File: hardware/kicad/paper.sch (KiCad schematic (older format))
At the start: 30 parts

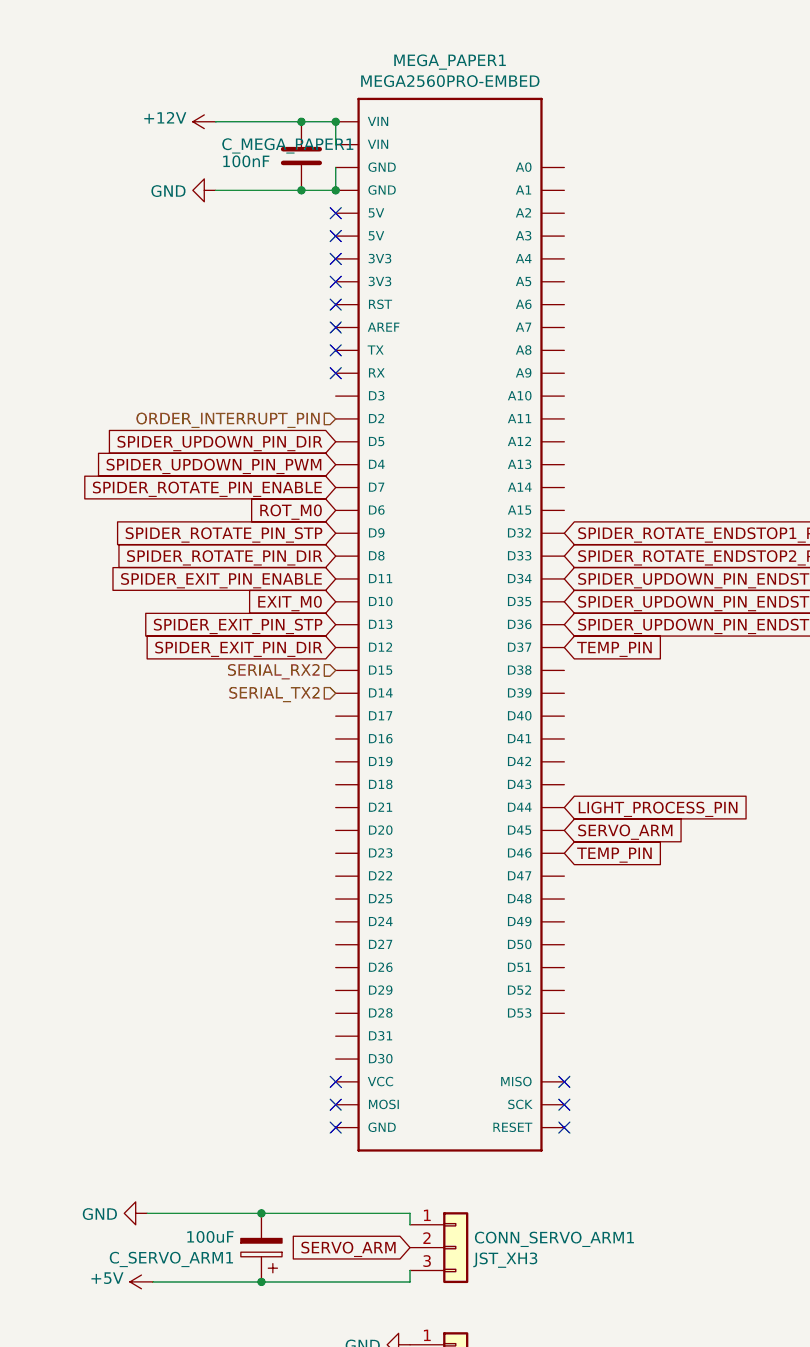
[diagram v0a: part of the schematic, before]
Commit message: correction schematic gilou
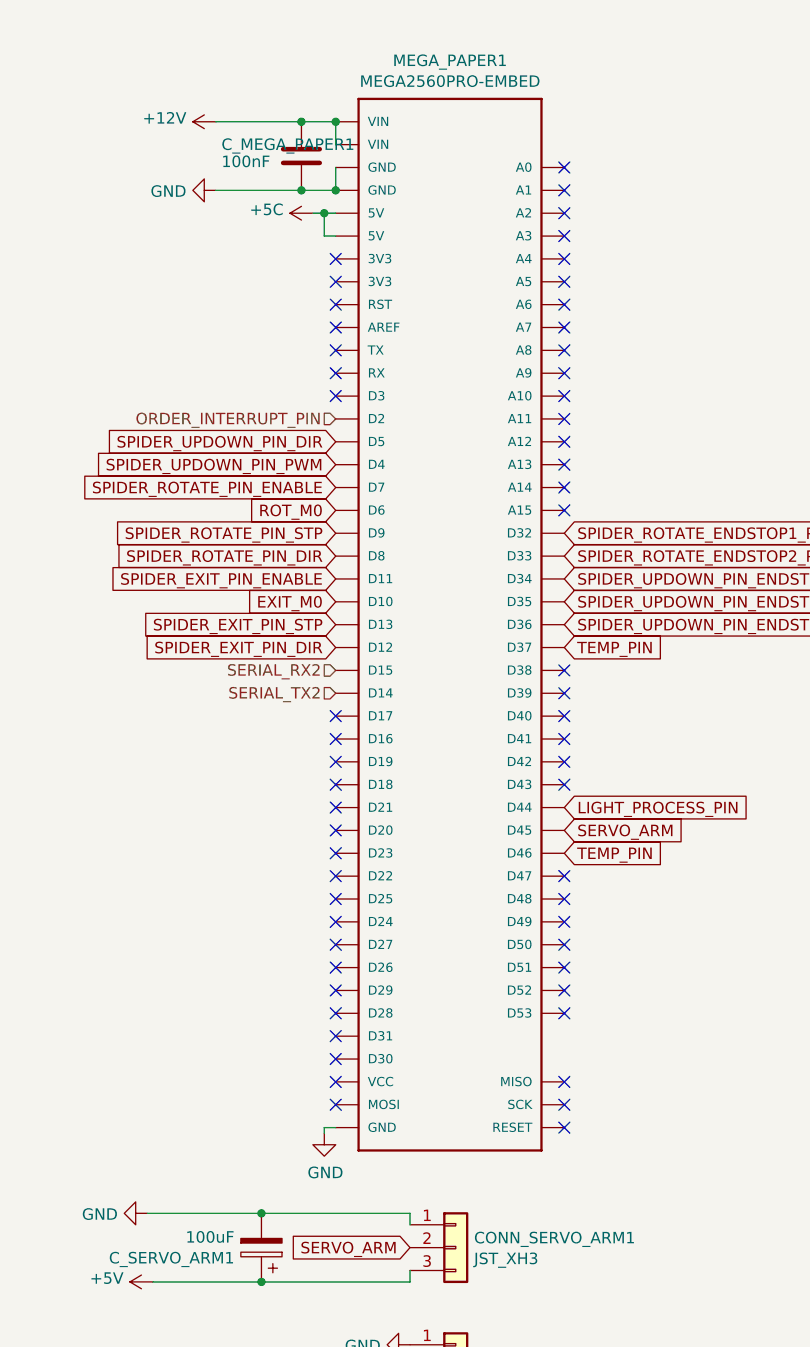
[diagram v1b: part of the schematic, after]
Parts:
- C_MEGA_PAPER1: footprint Capacitor_THT:C_Disc_D3.0mm_W1.6mm_P2.50mm -> Capacitor_THT:C_Rect_L7.2mm_W2.5mm_P5.00mm_FKS2_FKP2_MKS2_MKP2
- R_SW_BOTTOM1, R_SW_MIDDLE1, R_SW_ROT1, R_SW_ROT2, R_SW_UP1: footprint Resistor_THT:R_Axial_DIN0309_L9.0mm_D3.2mm_P12.70mm_Horizontal -> Resistor_THT:R_Axial_DIN0207_L6.3mm_D2.5mm_P10.16mm_Horizontal
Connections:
- net +5C: now reaches MEGA_PAPER1.5V
- no-connect marks 16 -> 59
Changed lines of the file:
@@
 F 0 "R_SW_ROT1" V 9379 925 50  0000 C CNN
 F 1 "560ohm 1/2W" V 9470 925 50  0000 C CNN
-F 2 "Resistor_THT:R_Axial_DIN0309_L9.0mm_D3.2mm_P12.70mm_Horizontal" H 9575 925 50  0001 C CNN
+F 2 "Resistor_THT:R_Axial_DIN0207_L6.3mm_D2.5mm_P10.16mm_Horizontal" H 9575 925 50  0001 C CNN
 F 3 "~" H 9575 925 50  0001 C CNN
 	1    9575 925
@@
 F 0 "R_SW_ROT2" V 9329 1775 50  0000 C CNN
 F 1 "560ohm 1/2W" V 9420 1775 50  0000 C CNN
-F 2 "Resistor_THT:R_Axial_DIN0309_L9.0mm_D3.2mm_P12.70mm_Horizontal" H 9525 1775 50  0001 C CNN
+F 2 "Resistor_THT:R_Axial_DIN0207_L6.3mm_D2.5mm_P10.16mm_Horizontal" H 9525 1775 50  0001 C CNN
 F 3 "~" H 9525 1775 50  0001 C CNN
 	1    9525 1775
@@
 F 0 "R_SW_UP1" V 9504 2725 50  0000 C CNN
 F 1 "560ohm 1/2W" V 9595 2725 50  0000 C CNN
-F 2 "Resistor_THT:R_Axial_DIN0309_L9.0mm_D3.2mm_P12.70mm_Horizontal" H 9700 2725 50  0001 C CNN
+F 2 "Resistor_THT:R_Axial_DIN0207_L6.3mm_D2.5mm_P10.16mm_Horizontal" H 9700 2725 50  0001 C CNN
 F 3 "~" H 9700 2725 50  0001 C CNN
 	1    9700 2725
@@
 F 0 "R_SW_MIDDLE1" V 9579 3750 50  0000 C CNN
 F 1 "560ohm 1/2W" V 9670 3750 50  0000 C CNN
-F 2 "Resistor_THT:R_Axial_DIN0309_L9.0mm_D3.2mm_P12.70mm_Horizontal" H 9775 3750 50  0001 C CNN
+F 2 "Resistor_THT:R_Axial_DIN0207_L6.3mm_D2.5mm_P10.16mm_Horizontal" H 9775 3750 50  0001 C CNN
 F 3 "~" H 9775 3750 50  0001 C CNN
 	1    9775 3750
@@
 F 0 "R_SW_BOTTOM1" V 9579 4550 50  0000 C CNN
 F 1 "560ohm 1/2W" V 9670 4550 50  0000 C CNN
-F 2 "Resistor_THT:R_Axial_DIN0309_L9.0mm_D3.2mm_P12.70mm_Horizontal" H 9775 4550 50  0001 C CNN
+F 2 "Resistor_THT:R_Axial_DIN0207_L6.3mm_D2.5mm_P10.16mm_Horizontal" H 9775 4550 50  0001 C CNN
 F 3 "~" H 9775 4550 50  0001 C CNN
 	1    9775 4550
@@
 Wire Wire Line
 	4900 6450 5550 6450
-NoConn ~ 5225 1775
-NoConn ~ 5225 1875
 NoConn ~ 5225 1975
 NoConn ~ 5225 2075
@@
 NoConn ~ 5225 5575
 NoConn ~ 5225 5675
-NoConn ~ 5225 5775
 NoConn ~ 6225 5575
 NoConn ~ 6225 5675
@@
 F 0 "C_MEGA_PAPER1" H 4725 1575 50  0000 L CNN
 F 1 "100nF" H 4725 1500 50  0000 L CNN
-F 2 "Capacitor_THT:C_Disc_D3.0mm_W1.6mm_P2.50mm" H 5113 1375 50  0001 C CNN
+F 2 "Capacitor_THT:C_Rect_L7.2mm_W2.5mm_P5.00mm_FKS2_FKP2_MKS2_MKP2" H 5113 1375 50  0001 C CNN
 F 3 "~" H 5075 1525 50  0001 C CNN
 	1    5075 1525
@@
 Wire Wire Line
 	1500 6200 1825 6200
+NoConn ~ 6225 1575
+NoConn ~ 6225 1675
+NoConn ~ 6225 1775
+NoConn ~ 6225 1875
+NoConn ~ 6225 1975
+NoConn ~ 6225 2075
+NoConn ~ 6225 2175
+NoConn ~ 6225 2275
+NoConn ~ 6225 2375
+NoConn ~ 6225 2475
+NoConn ~ 6225 2575
+NoConn ~ 6225 2675
+NoConn ~ 6225 2775
+NoConn ~ 6225 2875
+NoConn ~ 6225 2975
+NoConn ~ 6225 3075
+NoConn ~ 6225 3775
+NoConn ~ 6225 3875
+NoConn ~ 6225 3975
+NoConn ~ 6225 4075
+NoConn ~ 6225 4175
+NoConn ~ 6225 4275
+NoConn ~ 6225 4675
+NoConn ~ 6225 4775
+NoConn ~ 6225 4875
+NoConn ~ 6225 4975
+NoConn ~ 6225 5075
+NoConn ~ 6225 5175
+NoConn ~ 6225 5275
+NoConn ~ 5225 5475
+NoConn ~ 5225 5375
+NoConn ~ 5225 5275
+NoConn ~ 5225 5175
+NoConn ~ 5225 5075
+NoConn ~ 5225 4975
+NoConn ~ 5225 4875
+NoConn ~ 5225 4775
+NoConn ~ 5225 4675
+NoConn ~ 5225 4575
+NoConn ~ 5225 4475
+NoConn ~ 5225 4375
+NoConn ~ 5225 4275
+NoConn ~ 5225 4075
+NoConn ~ 5225 3975
+NoConn ~ 5225 4175
+NoConn ~ 5225 2575
+$Comp
+L power:GND #PWR0209
+U 1 1 5E497F5C
+P 5175 5800
+F 0 "#PWR0209" H 5175 5550 50  0001 C CNN
+F 1 "GND" H 5180 5627 50  0000 C CNN
+F 2 "" H 5175 5800 50  0001 C CNN
+F 3 "" H 5175 5800 50  0001 C CNN
+	1    5175 5800
+	1    0    0    -1
+$EndComp
+Wire Wire Line
+	5175 5800 5175 5775
+Wire Wire Line
+	5175 5775 5225 5775
+$Comp
+L power:+5C #PWR?
+U 1 1 5E4E76A1
+P 5125 1775
+AR Path="/5E3BF423/5E4E76A1" Ref="#PWR?"  Part="1"
+AR Path="/5E432787/5E4E76A1" Ref="#PWR0212"  Part="1"
+F 0 "#PWR0212" H 5125 1625 50  0001 C CNN
+F 1 "+5C" V 5140 1903 50  0000 L CNN
+F 2 "" H 5125 1775 50  0001 C CNN
+F 3 "" H 5125 1775 50  0001 C CNN
+	1    5125 1775
+	0    -1   -1   0
+$EndComp
+Wire Wire Line
+	5125 1775 5175 1775
+Wire Wire Line
+	5225 1875 5175 1875
+Wire Wire Line
+	5175 1875 5175 1775
+Connection ~ 5175 1775
+Wire Wire Line
+	5175 1775 5225 1775
 $EndSCHEMATC

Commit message: update, gilou dans la place
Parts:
- added CONN_FAN1: JST_XH2, Connector_JST:JST_XH_S2B-XH-A-1_1x02_P2.50mm_Horizontal, symbol 1nofilterbooth:Conn_01x02-Connector_Generic
- added C_AUX3: 680uF, Capacitor_THT:CP_Radial_D8.0mm_P3.50mm, symbol 1nofilterbooth:CP-Device
- added Q_AUX2: TIP120, Package_TO_SOT_THT:TO-220-3_Vertical, symbol 1nofilterbooth:TIP120-Transistor_BJT
- added R_FLASH4: 2.2k 1/2W, Resistor_THT:R_Axial_DIN0207_L6.3mm_D2.5mm_P10.16mm_Horizontal, symbol 1nofilterbooth:R_Small-Device
- CONN_DC1, CONN_SW_BOTTOM1, CONN_SW_MIDDLE1, CONN_SW_UP1: footprint Connector_JST:JST_XH_S2B-XH-A_1x02_P2.50mm_Horizontal -> Connector_JST:JST_XH_S2B-XH-A-1_1x02_P2.50mm_Horizontal
- CONN_LGHT_PROCESS1, CONN_SERVO_ARM1, CONN_SW_ROT1, CONN_SW_ROT2, CONN_TEMP1: footprint Connector_JST:JST_XH_S3B-XH-A_1x03_P2.50mm_Horizontal -> Connector_JST:JST_XH_S3B-XH-A-1_1x03_P2.50mm_Horizontal
- CONN_STEP_EXIT1, CONN_STEP_ROT1: value Conn_01x04 -> JST_XH4; footprint Connector_JST:JST_XH_S4B-XH-A_1x04_P2.50mm_Horizontal -> Connector_JST:JST_XH_S4B-XH-A-1_1x04_P2.50mm_Horizontal
- C_LIGHT_PROCESS1: value 1000uF -> 100uF; footprint Capacitor_THT:CP_Radial_D10.0mm_P5.00mm -> Capacitor_THT:CP_Radial_D6.3mm_P2.50mm
- C_ROT1, C_SERVO_ARM1, C_STEP1: footprint Capacitor_THT:CP_Radial_D10.0mm_P5.00mm -> Capacitor_THT:CP_Radial_D6.3mm_P2.50mm
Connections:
- net +12V: now also CONN_FAN1.1 (Pin_1), C_AUX3.2
- net GND: now also C_AUX3.1, Q_AUX2.3 (E)
- net FAN_PIN: now reaches MEGA_PAPER1.D39
- net FAN_PIN: now also R_FLASH4.2
- net at DRV_DC1.A: now also CONN_DC1.1 (Pin_1); no longer CONN_DC1.2 (Pin_2)
- net at DRV_DC1.B: now also CONN_DC1.2 (Pin_2); no longer CONN_DC1.1 (Pin_1)
- net +5C: no longer names the net of MEGA_PAPER1.5V
- new net: CONN_FAN1.2 (Pin_2), Q_AUX2.2 (C)
- new net: Q_AUX2.1 (B), R_FLASH4.1
- no-connect marks 59 -> 60
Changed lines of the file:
@@
 AR Path="/5E432787/5E421575" Ref="CONN_STEP_ROT1"  Part="1"
 F 0 "CONN_STEP_ROT1" H 1243 1325 50  0000 C CNN
-F 1 "Conn_01x04" H 1243 1416 50  0000 C CNN
-F 2 "Connector_JST:JST_XH_S4B-XH-A_1x04_P2.50mm_Horizontal" H 1325 1750 50  0001 C CNN
+F 1 "JST_XH4" H 1243 1416 50  0000 C CNN
+F 2 "Connector_JST:JST_XH_S4B-XH-A-1_1x04_P2.50mm_Horizontal" H 1325 1750 50  0001 C CNN
 F 3 "~" H 1325 1750 50  0001 C CNN
 	1    1325 1750
@@
 F 0 "C_ROT1" H 2643 2596 50  0000 L CNN
 F 1 "100uF" H 2643 2505 50  0000 L CNN
-F 2 "Capacitor_THT:CP_Radial_D10.0mm_P5.00mm" H 2563 2400 50  0001 C CNN
+F 2 "Capacitor_THT:CP_Radial_D6.3mm_P2.50mm" H 2563 2400 50  0001 C CNN
 F 3 "~" H 2525 2550 50  0001 C CNN
 	1    2525 2550
@@
 AR Path="/5E432787/5E43ED6E" Ref="CONN_STEP_EXIT1"  Part="1"
 F 0 "CONN_STEP_EXIT1" H 1193 3475 50  0000 C CNN
-F 1 "Conn_01x04" H 1193 3566 50  0000 C CNN
-F 2 "Connector_JST:JST_XH_S4B-XH-A_1x04_P2.50mm_Horizontal" H 1275 3900 50  0001 C CNN
+F 1 "JST_XH4" H 1193 3566 50  0000 C CNN
+F 2 "Connector_JST:JST_XH_S4B-XH-A-1_1x04_P2.50mm_Horizontal" H 1275 3900 50  0001 C CNN
 F 3 "~" H 1275 3900 50  0001 C CNN
 	1    1275 3900
@@
 F 0 "CONN_SW_ROT2" H 10205 2017 50  0000 L CNN
 F 1 "JST_XH3" H 10205 1926 50  0000 L CNN
-F 2 "Connector_JST:JST_XH_S3B-XH-A_1x03_P2.50mm_Horizontal" H 10125 1975 50  0001 C CNN
+F 2 "Connector_JST:JST_XH_S3B-XH-A-1_1x03_P2.50mm_Horizontal" H 10125 1975 50  0001 C CNN
 F 3 "~" H 10125 1975 50  0001 C CNN
 	1    10125 1975
@@
 F 0 "CONN_SW_ROT1" H 10255 1167 50  0000 L CNN
 F 1 "JST_XH3" H 10255 1076 50  0000 L CNN
-F 2 "Connector_JST:JST_XH_S3B-XH-A_1x03_P2.50mm_Horizontal" H 10175 1125 50  0001 C CNN
+F 2 "Connector_JST:JST_XH_S3B-XH-A-1_1x03_P2.50mm_Horizontal" H 10175 1125 50  0001 C CNN
 F 3 "~" H 10175 1125 50  0001 C CNN
 	1    10175 1125
@@
 F 0 "CONN_SW_UP1" H 10180 2917 50  0000 L CNN
 F 1 "JST_XH2" H 10180 2826 50  0000 L CNN
-F 2 "Connector_JST:JST_XH_S2B-XH-A_1x02_P2.50mm_Horizontal" H 10100 2925 50  0001 C CNN
+F 2 "Connector_JST:JST_XH_S2B-XH-A-1_1x02_P2.50mm_Horizontal" H 10100 2925 50  0001 C CNN
 F 3 "~" H 10100 2925 50  0001 C CNN
 	1    10100 2925
@@
 F 0 "CONN_SW_MIDDLE1" H 10255 3942 50  0000 L CNN
 F 1 "JST_XH2" H 10255 3851 50  0000 L CNN
-F 2 "Connector_JST:JST_XH_S2B-XH-A_1x02_P2.50mm_Horizontal" H 10175 3950 50  0001 C CNN
+F 2 "Connector_JST:JST_XH_S2B-XH-A-1_1x02_P2.50mm_Horizontal" H 10175 3950 50  0001 C CNN
 F 3 "~" H 10175 3950 50  0001 C CNN
 	1    10175 3950
@@
 F 0 "CONN_SW_BOTTOM1" H 10255 4742 50  0000 L CNN
 F 1 "JST_XH2" H 10255 4651 50  0000 L CNN
-F 2 "Connector_JST:JST_XH_S2B-XH-A_1x02_P2.50mm_Horizontal" H 10175 4750 50  0001 C CNN
+F 2 "Connector_JST:JST_XH_S2B-XH-A-1_1x02_P2.50mm_Horizontal" H 10175 4750 50  0001 C CNN
 F 3 "~" H 10175 4750 50  0001 C CNN
 	1    10175 4750
@@
 F 0 "CONN_TEMP1" H 5830 6867 50  0000 L CNN
 F 1 "JST_XH3" H 5830 6776 50  0000 L CNN
-F 2 "Connector_JST:JST_XH_S3B-XH-A_1x03_P2.50mm_Horizontal" H 5750 6825 50  0001 C CNN
+F 2 "Connector_JST:JST_XH_S3B-XH-A-1_1x03_P2.50mm_Horizontal" H 5750 6825 50  0001 C CNN
 F 3 "~" H 5750 6825 50  0001 C CNN
 	1    5750 6825
@@
 F 0 "CONN_LGHT_PROCESS1" H 5830 7517 50  0000 L CNN
 F 1 "JST_XH3" H 5830 7426 50  0000 L CNN
-F 2 "Connector_JST:JST_XH_S3B-XH-A_1x03_P2.50mm_Horizontal" H 5750 7475 50  0001 C CNN
+F 2 "Connector_JST:JST_XH_S3B-XH-A-1_1x03_P2.50mm_Horizontal" H 5750 7475 50  0001 C CNN
 F 3 "~" H 5750 7475 50  0001 C CNN
 	1    5750 7475
@@
 F 0 "C_STEP1" H 2593 4746 50  0000 L CNN
 F 1 "100uF" H 2593 4655 50  0000 L CNN
-F 2 "Capacitor_THT:CP_Radial_D10.0mm_P5.00mm" H 2513 4550 50  0001 C CNN
+F 2 "Capacitor_THT:CP_Radial_D6.3mm_P2.50mm" H 2513 4550 50  0001 C CNN
 F 3 "~" H 2475 4700 50  0001 C CNN
 	1    2475 4700
@@
 AR Path="/5E432787/5E480053" Ref="C_LIGHT_PROCESS1"  Part="1"
 F 0 "C_LIGHT_PROCESS1" H 4743 7521 50  0000 L CNN
-F 1 "1000uF" H 4743 7430 50  0000 L CNN
-F 2 "Capacitor_THT:CP_Radial_D10.0mm_P5.00mm" H 4663 7325 50  0001 C CNN
+F 1 "100uF" H 4743 7430 50  0000 L CNN
+F 2 "Capacitor_THT:CP_Radial_D6.3mm_P2.50mm" H 4663 7325 50  0001 C CNN
 F 3 "~" H 4625 7475 50  0001 C CNN
 	1    4625 7475
@@
 F 0 "CONN_SERVO_ARM1" H 5830 6342 50  0000 L CNN
 F 1 "JST_XH3" H 5830 6251 50  0000 L CNN
-F 2 "Connector_JST:JST_XH_S3B-XH-A_1x03_P2.50mm_Horizontal" H 5750 6300 50  0001 C CNN
+F 2 "Connector_JST:JST_XH_S3B-XH-A-1_1x03_P2.50mm_Horizontal" H 5750 6300 50  0001 C CNN
 F 3 "~" H 5750 6300 50  0001 C CNN
 	1    5750 6300
@@
 F 0 "C_SERVO_ARM1" H 5018 6346 50  0000 L CNN
 F 1 "100uF" H 5018 6255 50  0000 L CNN
-F 2 "Capacitor_THT:CP_Radial_D10.0mm_P5.00mm" H 4938 6150 50  0001 C CNN
+F 2 "Capacitor_THT:CP_Radial_D6.3mm_P2.50mm" H 4938 6150 50  0001 C CNN
 F 3 "~" H 4900 6300 50  0001 C CNN
 	1    4900 6300
@@
 Wire Wire Line
 	4900 6450 5550 6450
-NoConn ~ 5225 1975
-NoConn ~ 5225 2075
 NoConn ~ 5225 2175
 NoConn ~ 5225 2275
@@
 L 1nofilterbooth:Conn_01x02-Connector_Generic CONN_SW_MIDDLE?
 U 1 1 5E5BAF8E
-P 1300 6200
+P 1300 6100
 AR Path="/5E5BAF8E" Ref="CONN_SW_MIDDLE?"  Part="1"
 AR Path="/5E3BF423/5E5BAF8E" Ref="CONN_SW_MIDDLE?"  Part="1"
 AR Path="/5E432787/5E5BAF8E" Ref="CONN_DC1"  Part="1"
-F 0 "CONN_DC1" H 1380 6192 50  0000 L CNN
-F 1 "JST_XH2" H 1380 6101 50  0000 L CNN
-F 2 "Connector_JST:JST_XH_S2B-XH-A_1x02_P2.50mm_Horizontal" H 1300 6200 50  0001 C CNN
-F 3 "~" H 1300 6200 50  0001 C CNN
-	1    1300 6200
-	-1   0    0    1
+F 0 "CONN_DC1" H 1380 6092 50  0000 L CNN
+F 1 "JST_XH2" H 1380 6001 50  0000 L CNN
+F 2 "Connector_JST:JST_XH_S2B-XH-A-1_1x02_P2.50mm_Horizontal" H 1300 6100 50  0001 C CNN
+F 3 "~" H 1300 6100 50  0001 C CNN
+	1    1300 6100
+	-1   0    0    -1
 $EndComp
 Wire Wire Line
@@
 NoConn ~ 6225 3075
 NoConn ~ 6225 3775
-NoConn ~ 6225 3875
 NoConn ~ 6225 3975
 NoConn ~ 6225 4075
@@
 	5175 5775 5225 5775
 $Comp
-L power:+5C #PWR?
-U 1 1 5E4E76A1
-P 5125 1775
-AR Path="/5E3BF423/5E4E76A1" Ref="#PWR?"  Part="1"
-AR Path="/5E432787/5E4E76A1" Ref="#PWR0212"  Part="1"
-F 0 "#PWR0212" H 5125 1625 50  0001 C CNN
-F 1 "+5C" V 5140 1903 50  0000 L CNN
-F 2 "" H 5125 1775 50  0001 C CNN
-F 3 "" H 5125 1775 50  0001 C CNN
-	1    5125 1775
-	0    -1   -1   0
-$EndComp
-Wire Wire Line
-	5125 1775 5175 1775
-Wire Wire Line
-	5225 1875 5175 1875
-Wire Wire Line
-	5175 1875 5175 1775
-Connection ~ 5175 1775
-Wire Wire Line
-	5175 1775 5225 1775
+L 1nofilterbooth:TIP120-Transistor_BJT Q_AUX?
+U 1 1 5E49604F
+P 10475 5825
+AR Path="/5E3BF423/5E49604F" Ref="Q_AUX?"  Part="1"
+AR Path="/5E432787/5E49604F" Ref="Q_AUX2"  Part="1"
+F 0 "Q_AUX2" H 10682 5871 50  0000 L CNN
+F 1 "TIP120" H 10682 5780 50  0000 L CNN
+F 2 "Package_TO_SOT_THT:TO-220-3_Vertical" H 10675 5750 50  0001 L CIN
+F 3 "http://www.fairchildsemi.com/ds/TI/TIP120.pdf" H 10475 5825 50  0001 L CNN
+	1    10475 5825
+	1    0    0    -1
+$EndComp
+$Comp
+L 1nofilterbooth:R_Small-Device R_FLASH?
+U 1 1 5E496055
+P 10175 5825
+AR Path="/5E3BF423/5E496055" Ref="R_FLASH?"  Part="1"
+AR Path="/5E432787/5E496055" Ref="R_FLASH4"  Part="1"
+F 0 "R_FLASH4" V 9979 5825 50  0000 C CNN
+F 1 "2.2k 1/2W" V 10070 5825 50  0000 C CNN
+F 2 "Resistor_THT:R_Axial_DIN0207_L6.3mm_D2.5mm_P10.16mm_Horizontal" H 10175 5825 50  0001 C CNN
+F 3 "~" H 10175 5825 50  0001 C CNN
+	1    10175 5825
+	0    1    1    0
+$EndComp
+$Comp
+L 1nofilterbooth:CP-Device C_AUX?
+U 1 1 5E49605B
+P 9650 5550
+AR Path="/5E3BF423/5E49605B" Ref="C_AUX?"  Part="1"
+AR Path="/5E432787/5E49605B" Ref="C_AUX3"  Part="1"
+F 0 "C_AUX3" H 9768 5596 50  0000 L CNN
+F 1 "680uF" H 9768 5505 50  0000 L CNN
+F 2 "Capacitor_THT:CP_Radial_D8.0mm_P3.50mm" H 9688 5400 50  0001 C CNN
+F 3 "~" H 9650 5550 50  0001 C CNN
+	1    9650 5550
+	-1   0    0    1
+$EndComp
+$Comp
+L 1nofilterbooth:GND-power #PWR?
+U 1 1 5E496061
+P 10575 6025
+AR Path="/5E3BF423/5E496061" Ref="#PWR?"  Part="1"
+AR Path="/5E432787/5E496061" Ref="#PWR0214"  Part="1"
+F 0 "#PWR0214" H 10575 5775 50  0001 C CNN
+F 1 "GND" H 10580 5852 50  0000 C CNN
+F 2 "" H 10575 6025 50  0001 C CNN
+F 3 "" H 10575 6025 50  0001 C CNN
+	1    10575 6025
+	1    0    0    -1
+$EndComp
+$Comp
+L 1nofilterbooth:+12V-power #PWR?
+U 1 1 5E49606C
+P 9650 5350
+AR Path="/5E3BF423/5E49606C" Ref="#PWR?"  Part="1"
+AR Path="/5E432787/5E49606C" Ref="#PWR0215"  Part="1"
+F 0 "#PWR0215" H 9650 5200 50  0001 C CNN
+F 1 "+12V" V 9665 5478 50  0000 L CNN
+F 2 "" H 9650 5350 50  0001 C CNN
+F 3 "" H 9650 5350 50  0001 C CNN
+	1    9650 5350
+	1    0    0    -1
+$EndComp
+Text Label 10075 5825 2    50   ~ 0
+FAN_PIN
+$Comp
+L 1nofilterbooth:Conn_01x02-Connector_Generic CONN_AUX?
+U 1 1 5E496049
+P 10975 5350
+AR Path="/5E496049" Ref="CONN_AUX?"  Part="1"
+AR Path="/5E3BF423/5E496049" Ref="CONN_AUX?"  Part="1"
+AR Path="/5E432787/5E496049" Ref="CONN_FAN1"  Part="1"
+F 0 "CONN_FAN1" V 10939 5162 50  0000 R CNN
+F 1 "JST_XH2" V 10848 5162 50  0000 R CNN
+F 2 "Connector_JST:JST_XH_S2B-XH-A-1_1x02_P2.50mm_Horizontal" H 10975 5350 50  0001 C CNN
+F 3 "~" H 10975 5350 50  0001 C CNN
+	1    10975 5350
+	1    0    0    -1
+$EndComp
+Wire Wire Line
+	10775 5350 9650 5350
+Wire Wire Line
+	9650 5400 9650 5350
+Connection ~ 9650 5350
+$Comp
+L 1nofilterbooth:GND-power #PWR?
+U 1 1 5E4A88C2
+P 9650 5750
+AR Path="/5E3BF423/5E4A88C2" Ref="#PWR?"  Part="1"
+AR Path="/5E432787/5E4A88C2" Ref="#PWR0216"  Part="1"
+F 0 "#PWR0216" H 9650 5500 50  0001 C CNN
+F 1 "GND" H 9655 5577 50  0000 C CNN
+F 2 "" H 9650 5750 50  0001 C CNN
+F 3 "" H 9650 5750 50  0001 C CNN
+	1    9650 5750
+	1    0    0    -1
+$EndComp
+Wire Wire Line
+	9650 5750 9650 5700
+Wire Wire Line
+	10575 5625 10575 5450
+Wire Wire Line
+	10575 5450 10775 5450
+Text Label 6325 3875 0    50   ~ 0
+FAN_PIN
+Wire Wire Line
+	6325 3875 6225 3875
+NoConn ~ 5225 1975
+NoConn ~ 5225 2075
+NoConn ~ 5225 1875
+NoConn ~ 5225 1775
 $EndSCHEMATC
